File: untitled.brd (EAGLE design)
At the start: 100 x 80 mm, 8 parts

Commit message: fixed wiring
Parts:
- moved U$1 4.27 mm to (51.2, 47.5)
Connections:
- net D1 renamed N$1
- removed net C7: U$1.C7
- removed net N$14: SV1.1, U$1.GND
- removed net N$16: TASTENLINKS.P$2, U$1.D3
- removed net N$17: TASTENLINKS.P$4, U$1.D2
- net D2: now also TASTENLINKS.P$4, U$1.D2
- net D3: now also TASTENLINKS.P$2, U$1.D3
- net D5: now also U$1.D5
- net GND: now also SV1.1, U$1.GND
- net N$2: now also U$1.B3
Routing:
- net N$2: track 150.5 -> 0.00 mm
- net B5: track 144.8 -> 0.00 mm
- net B4: track 135.7 -> 0.00 mm
- net B1: track 133.7 -> 0.00 mm, vias 1 -> 0
- net B2: track 126.2 -> 0.00 mm
- net C5: track 122.6 -> 0.00 mm
- net B0: track 115.2 -> 0.00 mm
- net C6: track 110.0 -> 0.00 mm
- net D7: track 106.1 -> 0.00 mm, vias 1 -> 0
- net C1: track 101.0 -> 0.00 mm, vias 1 -> 0
- net C4: track 93.7 -> 0.00 mm
- net C0: track 92.7 -> 0.00 mm, vias 1 -> 0
- net D6: track 89.7 -> 0.00 mm
- net B6: track 79.2 -> 0.00 mm
- net D4: track 69.0 -> 0.00 mm
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
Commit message: renamed nets to pinout
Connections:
- net N$1 renamed D1
- net N$18 renamed D0
- net N$2 renamed B3
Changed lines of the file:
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@@
 <wire x1="13.97" y1="7.62" x2="43.63" y2="25.91" width="0" layer="19" extent="1-1"/>
 </signal>
-<signal name="N$18">
+<signal name="D0">
 <contactref element="U$1" pad="D0"/>
 <contactref element="TASTENLINKS" pad="P$6"/>
 <wire x1="58.87" y1="28.45" x2="87.1" y2="37.5" width="0" layer="19" extent="1-1"/>
 </signal>
-<signal name="N$2">
+<signal name="B3">
 <contactref element="TOPRECHTS" pad="P$8"/>
 <contactref element="TASTENLINKS" pad="P$10"/>
@@
 <wire x1="11.65" y1="70" x2="10" y2="37.5" width="0" layer="19" extent="1-1"/>
 </signal>
-<signal name="N$1">
+<signal name="D1">
 <contactref element="TASTENLINKS" pad="P$7"/>
 <contactref element="U$1" pad="D1"/>

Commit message: half-optimized
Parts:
- removed SV1: (no value), con-lstb:MA03-1
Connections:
- new net N$1: U$1.GND
- net GND: no longer SV1.1, U$1.GND
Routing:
- net B5: track 0.00 -> 156.1 mm
- net B2: track 0.00 -> 155.1 mm
- net B6: track 0.00 -> 130.0 mm
- net B1: track 0.00 -> 128.4 mm
- net B3: track 0.00 -> 119.9 mm, vias 0 -> 1
- net B4: track 0.00 -> 119.4 mm, vias 0 -> 1
- net B0: track 0.00 -> 118.4 mm
- net D7: track 0.00 -> 111.7 mm, vias 0 -> 1
- net C5: track 0.00 -> 111.6 mm
- net C6: track 0.00 -> 104.8 mm
- net C1: track 0.00 -> 94.2 mm
- net C0: track 0.00 -> 93.7 mm, vias 0 -> 1
- net C4: track 0.00 -> 90.4 mm, vias 0 -> 1
- net D6: track 0.00 -> 78.4 mm, vias 0 -> 1
- net D4: track 0.00 -> 72.8 mm
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
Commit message: board finished
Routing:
- net B6: track 130.0 -> 83.1 mm
- net D4: track 72.8 -> 106.5 mm
- net D6: track 78.4 -> 109.1 mm, vias 1 -> 0
- net B2: track 155.1 -> 133.1 mm
- net C5: track 111.6 -> 127.9 mm
- net D2: track 57.2 -> 70.3 mm, vias 1 -> 0
- net B1: track 128.4 -> 122.1 mm
- net D5: track 48.9 -> 54.8 mm
- net C3: track 64.9 -> 70.4 mm, vias 1 -> 0
- net D3: track 67.5 -> 72.4 mm
- net C0: track 93.7 -> 98.2 mm
- net B5: track 156.1 -> 151.9 mm
- net C4: track 90.4 -> 86.7 mm, vias 1 -> 0
- net D1: track 47.4 -> 43.8 mm
- net D7: track 111.7 -> 108.2 mm, vias 1 -> 0
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
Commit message: removed another via…
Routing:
- net B0: track 116.6 -> 121.3 mm, vias 1 -> 0
- added copper zone on layer 1, net GND
- added copper zone on layer 16, net GND
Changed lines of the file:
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@@
 <signal name="GND">
 <contactref element="U$1" pad="GRND1"/>
+<polygon width="0.254" layer="1" orphans="yes">
+<vertex x="0" y="0"/>
+<vertex x="100" y="0"/>
+<vertex x="100" y="80"/>
+<vertex x="0" y="80"/>
+</polygon>
+<polygon width="0.254" layer="16" orphans="yes">
+<vertex x="0" y="80"/>
+<vertex x="100" y="80"/>
+<vertex x="100" y="0"/>
+<vertex x="0" y="0"/>
+</polygon>
 </signal>
 <signal name="VCC">
@@
 <contactref element="TASTENRECHTS" pad="P$10"/>
 <contactref element="U$1" pad="B0"/>
-<wire x1="88.75" y1="43.75" x2="87.5" y2="45" width="0.254" layer="16"/>
-<wire x1="87.5" y1="45" x2="63.75" y2="45" width="0.254" layer="16"/>
-<wire x1="63.75" y1="45" x2="61.25" y2="42.5" width="0.254" layer="1"/>
-<wire x1="61.25" y1="42.5" x2="44.98" y2="42.5" width="0.254" layer="1"/>
-<wire x1="87.5" y1="45" x2="93.75" y2="51.25" width="0.254" layer="16"/>
-<wire x1="93.75" y1="51.25" x2="93.75" y2="73.75" width="0.254" layer="16"/>
+<wire x1="88.75" y1="43.75" x2="85" y2="47.5" width="0.254" layer="16"/>
+<wire x1="85" y1="47.5" x2="50" y2="47.5" width="0.254" layer="16"/>
+<wire x1="85" y1="47.5" x2="93.75" y2="55" width="0.254" layer="16"/>
+<wire x1="93.75" y1="55" x2="93.75" y2="73.75" width="0.254" layer="16"/>
 <wire x1="93.75" y1="73.75" x2="91.25" y2="76.25" width="0.254" layer="16"/>
 <wire x1="91.25" y1="76.25" x2="88.75" y2="76.25" width="0.254" layer="16"/>
-<via x="63.75" y="45" extent="1-16" drill="0.696"/>
 <wire x1="43.63" y1="41.15" x2="11.75" y2="41.15" width="0.254" layer="16"/>
 <wire x1="11.75" y1="41.15" x2="11.65" y2="41.25" width="0.254" layer="16"/>
-<wire x1="44.98" y1="42.5" x2="43.63" y2="41.15" width="0.254" layer="1"/>
+<wire x1="43.63" y1="41.15" x2="49.9" y2="41.15" width="0.254" layer="16"/>
+<wire x1="49.9" y1="41.15" x2="50" y2="41.25" width="0.254" layer="16"/>
+<wire x1="50" y1="41.25" x2="50" y2="47.5" width="0.254" layer="16"/>
 </signal>
 <signal name="B1">

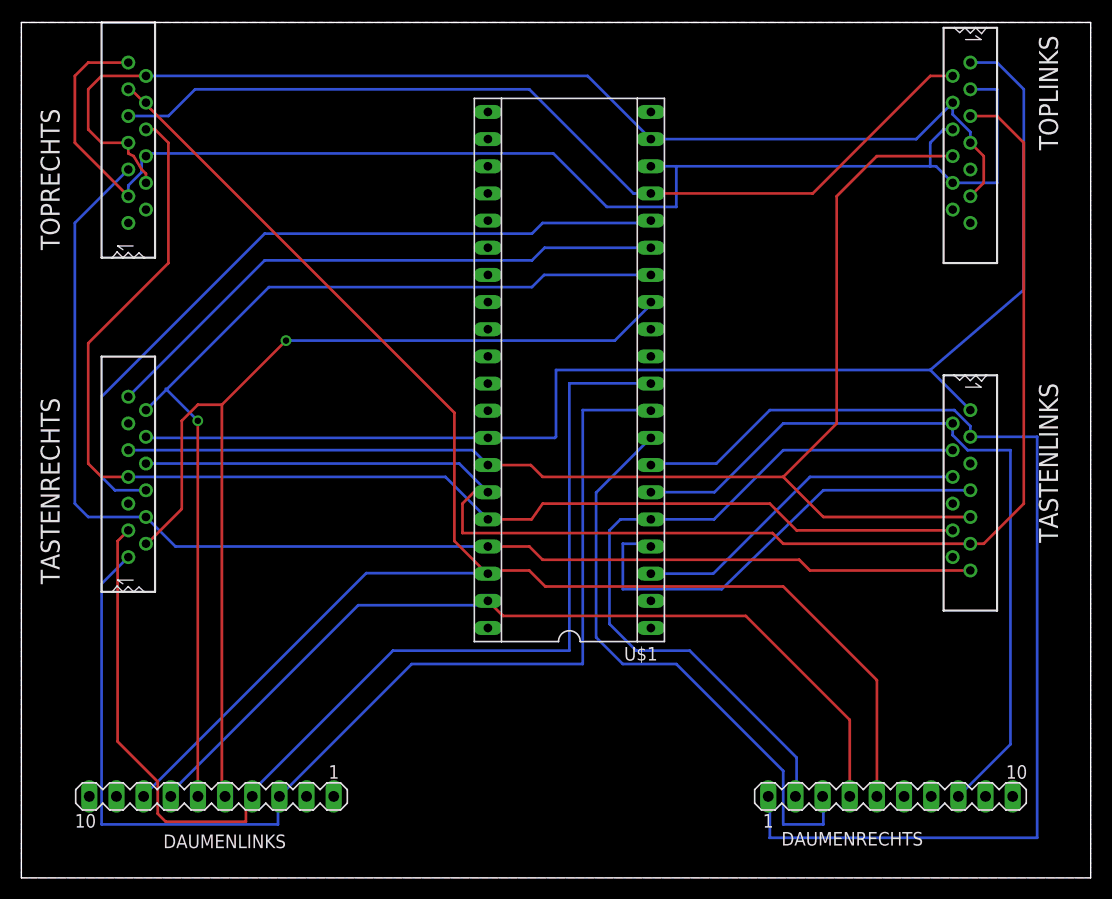
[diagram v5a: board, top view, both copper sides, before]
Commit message: less diagonal-routing below molex
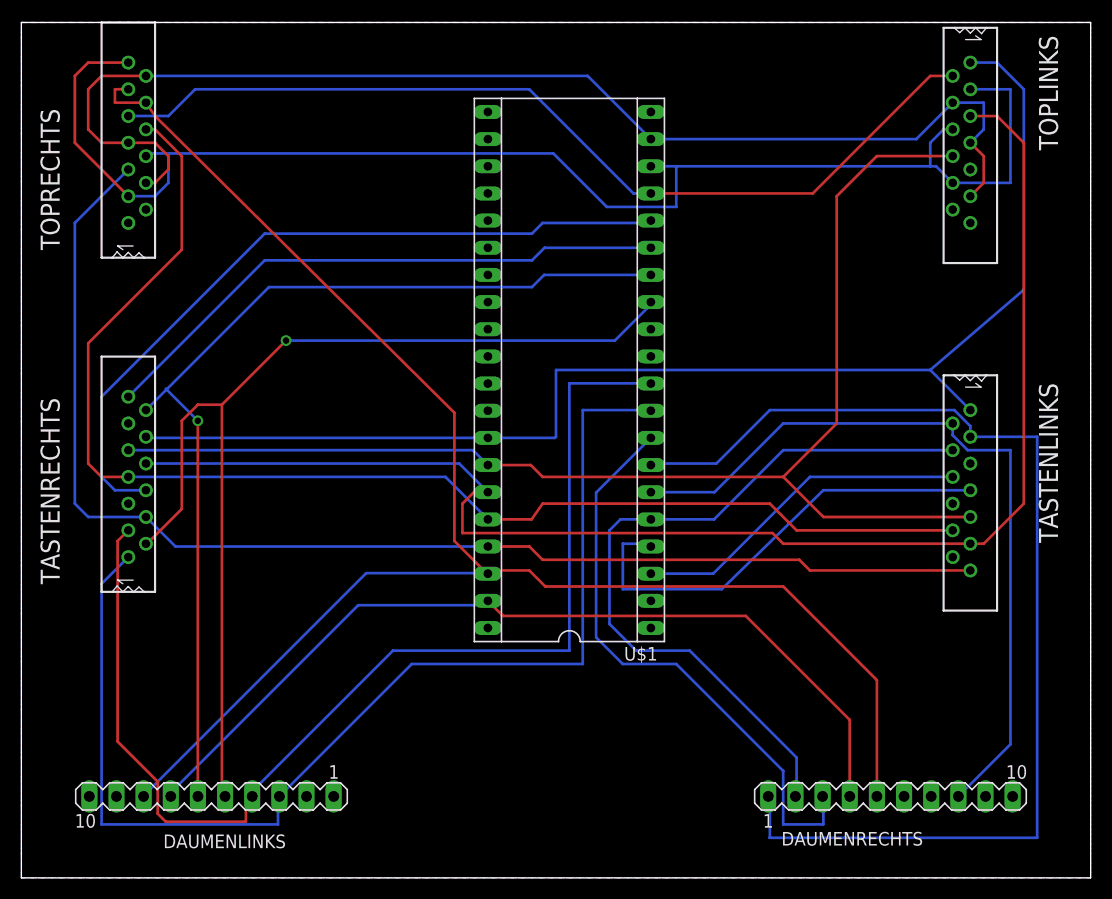
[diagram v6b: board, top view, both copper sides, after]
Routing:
- net C6: track 108.1 -> 114.6 mm
- net C5: track 127.9 -> 132.9 mm
- net B5: track 151.9 -> 155.2 mm
- net B3: track 120.5 -> 121.6 mm
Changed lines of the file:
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@@
 <wire x1="58.87" y1="69.09" x2="83.69" y2="69.09" width="0.254" layer="16"/>
 <wire x1="83.69" y1="69.09" x2="87.1" y2="72.5" width="0.254" layer="16"/>
-<wire x1="87.1" y1="72.5" x2="87.1" y2="71.4" width="0.254" layer="16"/>
-<wire x1="87.1" y1="71.4" x2="88.75" y2="69.75" width="0.254" layer="16"/>
-<wire x1="88.75" y1="69.75" x2="88.75" y2="68.75" width="0.254" layer="16"/>
+<wire x1="87.1" y1="72.5" x2="90" y2="72.5" width="0.254" layer="16"/>
+<wire x1="90" y1="72.5" x2="90" y2="70" width="0.254" layer="16"/>
+<wire x1="90" y1="70" x2="88.75" y2="68.75" width="0.254" layer="16"/>
 <wire x1="88.75" y1="68.75" x2="90" y2="67.5" width="0.254" layer="1"/>
 <wire x1="90" y1="67.5" x2="90" y2="65" width="0.254" layer="1"/>
 <wire x1="90" y1="65" x2="88.75" y2="63.75" width="0.254" layer="1"/>
-<wire x1="11.65" y1="65" x2="11.65" y2="65.85" width="0.254" layer="1"/>
-<wire x1="11.65" y1="65.85" x2="11.25" y2="66.25" width="0.254" layer="1"/>
-<wire x1="11.25" y1="66.25" x2="10.5" y2="67.5" width="0.254" layer="1"/>
-<wire x1="10.5" y1="67.5" x2="10" y2="67.75" width="0.254" layer="1"/>
-<wire x1="10" y1="67.75" x2="10" y2="68.75" width="0.254" layer="1"/>
+<wire x1="11.65" y1="65" x2="12.5" y2="65" width="0.254" layer="1"/>
+<wire x1="12.5" y1="65" x2="13.75" y2="66.25" width="0.254" layer="1"/>
+<wire x1="13.75" y1="66.25" x2="13.75" y2="67.5" width="0.254" layer="1"/>
+<wire x1="13.75" y1="67.5" x2="12.5" y2="68.75" width="0.254" layer="1"/>
+<wire x1="12.5" y1="68.75" x2="10" y2="68.75" width="0.254" layer="1"/>
 <wire x1="10" y1="68.75" x2="7.5" y2="68.75" width="0.254" layer="1"/>
 <wire x1="7.5" y1="68.75" x2="6.25" y2="70" width="0.254" layer="1"/>
@@
 <wire x1="85.55" y1="66.55" x2="85" y2="66.55" width="0.254" layer="16"/>
 <wire x1="85" y1="66.55" x2="61.25" y2="66.55" width="0.254" layer="16"/>
-<wire x1="88.75" y1="73.75" x2="91.25" y2="73.75" width="0.254" layer="16"/>
-<wire x1="91.25" y1="73.75" x2="91.25" y2="65" width="0.254" layer="16"/>
-<wire x1="91.25" y1="65" x2="87.1" y2="65" width="0.254" layer="16"/>
+<wire x1="88.75" y1="73.75" x2="92.5" y2="73.75" width="0.254" layer="16"/>
+<wire x1="92.5" y1="73.75" x2="92.5" y2="65" width="0.254" layer="16"/>
+<wire x1="92.5" y1="65" x2="87.1" y2="65" width="0.254" layer="16"/>
 <wire x1="87.1" y1="70" x2="86.25" y2="70" width="0.254" layer="16"/>
 <wire x1="86.25" y1="70" x2="85" y2="68.75" width="0.254" layer="16"/>
 <wire x1="85" y1="68.75" x2="85" y2="66.55" width="0.254" layer="16"/>
 <wire x1="11.65" y1="67.5" x2="11.9" y2="67.75" width="0.254" layer="16"/>
-<wire x1="11.65" y1="67.5" x2="11.25" y2="67.1" width="0.254" layer="16"/>
-<wire x1="11.25" y1="67.1" x2="11.25" y2="66" width="0.254" layer="16"/>
-<wire x1="11.25" y1="66" x2="10" y2="64.75" width="0.254" layer="16"/>
-<wire x1="10" y1="64.75" x2="10" y2="63.75" width="0.254" layer="16"/>
+<wire x1="13.75" y1="65" x2="12.5" y2="63.75" width="0.254" layer="16"/>
+<wire x1="12.5" y1="63.75" x2="10" y2="63.75" width="0.254" layer="16"/>
 <wire x1="11.9" y1="67.75" x2="49.75" y2="67.75" width="0.254" layer="16"/>
 <wire x1="49.75" y1="67.75" x2="54.75" y2="62.75" width="0.254" layer="16"/>
@@
 <wire x1="54.75" y1="62.75" x2="61.25" y2="62.75" width="0.254" layer="16"/>
 <wire x1="61.25" y1="62.75" x2="61.25" y2="66.55" width="0.254" layer="16"/>
+<wire x1="13.75" y1="67.6" x2="13.75" y2="65" width="0.254" layer="16"/>
+<wire x1="13.75" y1="67.6" x2="11.9" y2="67.75" width="0" layer="19" extent="16-16"/>
 </signal>
 <signal name="C4">
@@
 <wire x1="47.5" y1="28.75" x2="43.93" y2="28.75" width="0.254" layer="1"/>
 <wire x1="43.93" y1="28.75" x2="43.63" y2="28.45" width="0.254" layer="1"/>
-<wire x1="10.5" y1="73.5" x2="11.25" y2="72.75" width="0.254" layer="1"/>
-<wire x1="11.25" y1="72.75" x2="11.65" y2="72.5" width="0.254" layer="1"/>
-<wire x1="10.5" y1="73.5" x2="10" y2="73.75" width="0.254" layer="1"/>
+<wire x1="8.75" y1="73.75" x2="8.75" y2="72.5" width="0.254" layer="1"/>
+<wire x1="8.75" y1="72.5" x2="11.65" y2="72.5" width="0.254" layer="1"/>
+<wire x1="8.75" y1="73.75" x2="10" y2="73.75" width="0.254" layer="1"/>
 <wire x1="32.25" y1="28.5" x2="12" y2="8.25" width="0.254" layer="16"/>
 <wire x1="43.5" y1="28.5" x2="32.25" y2="28.5" width="0.254" layer="16"/>
 <wire x1="12" y1="8.25" x2="11.43" y2="7.62" width="0.254" layer="16"/>
 <wire x1="43.5" y1="28.5" x2="43.63" y2="28.45" width="0.254" layer="16"/>
-<wire x1="40.5" y1="43.5" x2="12" y2="72" width="0.254" layer="1"/>
+<wire x1="40.5" y1="43.5" x2="12.5" y2="71.25" width="0.254" layer="1"/>
 <wire x1="40.5" y1="31.5" x2="40.5" y2="43.5" width="0.254" layer="1"/>
 <wire x1="43.5" y1="28.5" x2="40.5" y2="31.5" width="0.254" layer="1"/>
-<wire x1="12" y1="72" x2="11.65" y2="72.5" width="0.254" layer="1"/>
+<wire x1="12.5" y1="71.25" x2="11.65" y2="72.5" width="0.254" layer="1"/>
 <wire x1="43.5" y1="28.5" x2="43.63" y2="28.45" width="0.254" layer="1"/>
 </signal>
@@
 <wire x1="47.72" y1="33.53" x2="43.63" y2="33.53" width="0.254" layer="1"/>
 <wire x1="11.65" y1="70" x2="12.5" y2="70" width="0.254" layer="1"/>
-<wire x1="12.5" y1="70" x2="13.75" y2="68.75" width="0.254" layer="1"/>
-<wire x1="13.75" y1="68.75" x2="13.75" y2="57.5" width="0.254" layer="1"/>
-<wire x1="13.75" y1="57.5" x2="6.25" y2="50" width="0.254" layer="1"/>
+<wire x1="12.5" y1="70" x2="15" y2="67.5" width="0.254" layer="1"/>
+<wire x1="15" y1="67.5" x2="15" y2="58.75" width="0.254" layer="1"/>
+<wire x1="15" y1="58.75" x2="6.25" y2="50" width="0.254" layer="1"/>
 <wire x1="6.25" y1="50" x2="6.25" y2="38.75" width="0.254" layer="1"/>
 <wire x1="6.25" y1="38.75" x2="7.5" y2="37.5" width="0.254" layer="1"/>
